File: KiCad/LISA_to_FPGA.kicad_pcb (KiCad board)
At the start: 2 copper layers, 77.7 x 29.5 mm, 16 parts, among them J1 Conn_01x02, J2 Conn_01x02, J3 Conn_01x40, U1 LM1117-3.3, U2 74LVC245A, U3 74LVC245A, U5 LISA

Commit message: more place and route
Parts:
- removed J3: Conn_01x40, Connector_FFC-FPC:Hirose_FH12-40S-0.5SH_1x40-1MP_P0.50mm_Horizontal
- removed the REF** at (133.3, 95.8)
- added U4: 74LVC245A, Package_SO:TSSOP-20_4.4x6.5mm_P0.65mm, F.Cu at (187.6, 85.9)
- added U6: LISA, LISA_to_FPGA:PLCC-84_THT-Socket-HAT, B.Cu at (166.8, 90.4)
- C3: footprint Capacitor_SMD:C_0805_2012Metric_Pad1.15x1.40mm_HandSolder -> Capacitor_SMD:C_0603_1608Metric_Pad1.08x0.95mm_HandSolder; moved to F.Cu
- C4, C5: footprint Capacitor_SMD:C_0805_2012Metric_Pad1.15x1.40mm_HandSolder -> Capacitor_SMD:C_0603_1608Metric_Pad1.08x0.95mm_HandSolder
- C6: footprint Capacitor_SMD:C_0805_2012Metric_Pad1.18x1.45mm_HandSolder -> Capacitor_SMD:C_0603_1608Metric_Pad1.08x0.95mm_HandSolder
- J1: value Conn_01x02 -> Conn_01x03; footprint Connector_PinHeader_2.54mm:PinHeader_1x02_P2.54mm_Horizontal -> Connector_PinHeader_2.54mm:PinHeader_1x03_P2.54mm_Horizontal
- J2: value Conn_01x02 -> Conn_01x40; footprint Connector_PinHeader_2.54mm:PinHeader_1x02_P2.54mm_Horizontal -> Connector_FFC-FPC:Hirose_FH12-40S-0.5SH_1x40-1MP_P0.50mm_Horizontal
- U5: value LISA -> 74LVC245A; footprint Package_LCC:PLCC-84_THT-Socket -> Package_SO:TSSOP-20_4.4x6.5mm_P0.65mm; moved to F.Cu
- moved C3 51.1 mm to (193.0, 99.0)
- moved C6 45.0 mm to (189.6, 73.5)
- moved C4 39.3 mm to (193.0, 92.3), turned to 90 degrees
- moved U2 39.1 mm to (187.6, 100.9)
- moved U1 38.6 mm to (191.8, 89.7)
- moved U3 36.5 mm to (187.6, 93.4)
- moved REF** 36.0 mm to (234.3, 93.4)
- moved C5 29.9 mm to (193.0, 84.0), turned to 90 degrees
- moved R1 23.2 mm to (193.9, 104.3)
- moved U5 13.4 mm to (187.6, 78.4), turned to 0 degrees
- moved J2 12.5 mm to (199.3, 94.4), turned to 90 degrees
- moved J1 5.59 mm to (191.3, 106.9)
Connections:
- J1 pad 2: Net-(J1-Pad2) -> HSYNC
- J2 pad 1: VSYNC -> /C14M_3V3
- J2 pad 2: HSYNC -> GND
- R1 pad 2: C14OUT -> C14OUT_3V3
- U2 pad 11: G7_3V3 -> C14OUT_3V3
- U2 pad 12: G6_3V3 -> VSYNC_3V3
- U2 pad 13: G5_3V3 -> HSYNC_3V3
- U2 pad 14: G4_3V3 -> PIXELSW_3V3
- U2 pad 15: R7_3V3 -> CSYNC_3V3
- U2 pad 16: R6_3V3 -> B7_3V3
- U2 pad 17: R5_3V3 -> B6_3V3
- U2 pad 18: R4_3V3 -> B5_3V3
- U2 pad 2: R4 -> B5
- U2 pad 3: R5 -> B6
- U2 pad 4: R6 -> B7
- U2 pad 5: R7 -> CSYNC
- U2 pad 6: G4 -> PIXELSW
- U2 pad 7: G5 -> HSYNC
- U2 pad 8: G6 -> VSYNC
- U2 pad 9: G7 -> C14OUT
- U3 pad 11: VSYNC_3V3 -> B4_3V3
- U3 pad 12: HSYNC_3V3 -> B3_3V3
- U3 pad 13: PIXELSW_3V3 -> B2_3V3
- U3 pad 14: CSYNC_3V3 -> B1_3V3
- U3 pad 15: B7_3V3 -> B0_3V3
- U3 pad 16: B6_3V3 -> G7_3V3
- U3 pad 17: B5_3V3 -> G6_3V3
- U3 pad 18: B4_3V3 -> G5_3V3
- U3 pad 2: B4 -> G5
- U3 pad 3: B5 -> G6
- U3 pad 4: B6 -> G7
- U3 pad 5: B7 -> B0
- U3 pad 6: CSYNC -> B1
- U3 pad 7: PIXELSW -> B2
- U3 pad 8: HSYNC -> B3
- U3 pad 9: VSYNC -> B4
- U5 pad 1: GND -> 3V3
- U5 pad 10: Net-(U5-Pad10) -> GND
- U5 pad 11: Net-(U5-Pad11) -> R4_3V3
- U5 pad 12: Net-(U5-Pad12) -> R3_3V3
- U5 pad 13: Net-(U5-Pad13) -> R2_3V3
- U5 pad 14: Net-(U5-Pad14) -> R1_3V3
- U5 pad 15: Net-(U5-Pad15) -> R0_3V3
- U5 pad 19: Net-(U5-Pad19) -> GND
- U5 pad 2: Net-(U5-Pad2) -> GND
- U5 pad 20: Net-(U5-Pad20) -> 3V3
- U5 pad 3: Net-(U5-Pad3) -> GND
- U5 pad 4: Net-(U5-Pad4) -> GND
- U5 pad 5: Net-(U5-Pad5) -> R0
- U5 pad 6: Net-(U5-Pad6) -> R1
- U5 pad 7: Net-(U5-Pad7) -> R2
- U5 pad 8: Net-(U5-Pad8) -> R3
- U5 pad 9: Net-(U5-Pad9) -> R4
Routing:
- net VCC: track 0.00 -> 69.7 mm
- net G4: track 0.00 -> 43.9 mm, vias 0 -> 1
- net G7: track 0.00 -> 40.5 mm, vias 0 -> 1
- net G3: track 0.00 -> 39.6 mm, vias 0 -> 1
- net R5: track 0.00 -> 36.3 mm
- net G5: track 0.00 -> 34.5 mm, vias 0 -> 1
- net R0: track 0.00 -> 33.8 mm
- net R3: track 0.00 -> 33.7 mm
- net G1: track 0.00 -> 33.7 mm, vias 0 -> 1
- net R7: track 0.00 -> 33.2 mm
- net G6: track 0.00 -> 33.2 mm, vias 0 -> 1
- net G2: track 0.00 -> 33.2 mm, vias 0 -> 1
- net B6: track 0.00 -> 33.0 mm, vias 0 -> 1
- net R4: track 0.00 -> 32.4 mm
- net R6: track 0.00 -> 32.4 mm
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- added copper zone on 3V3.Cu, net 3V3
- added copper zone on GND.Cu, net GND
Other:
- board size 77.7 x 29.5 mm -> 54.9 x 37 mm
- copper layers 2 -> 4
- board text added: "LISA to FPGA"
- board text removed: "CDAC"
- board text removed: "DENISE to FPGA"

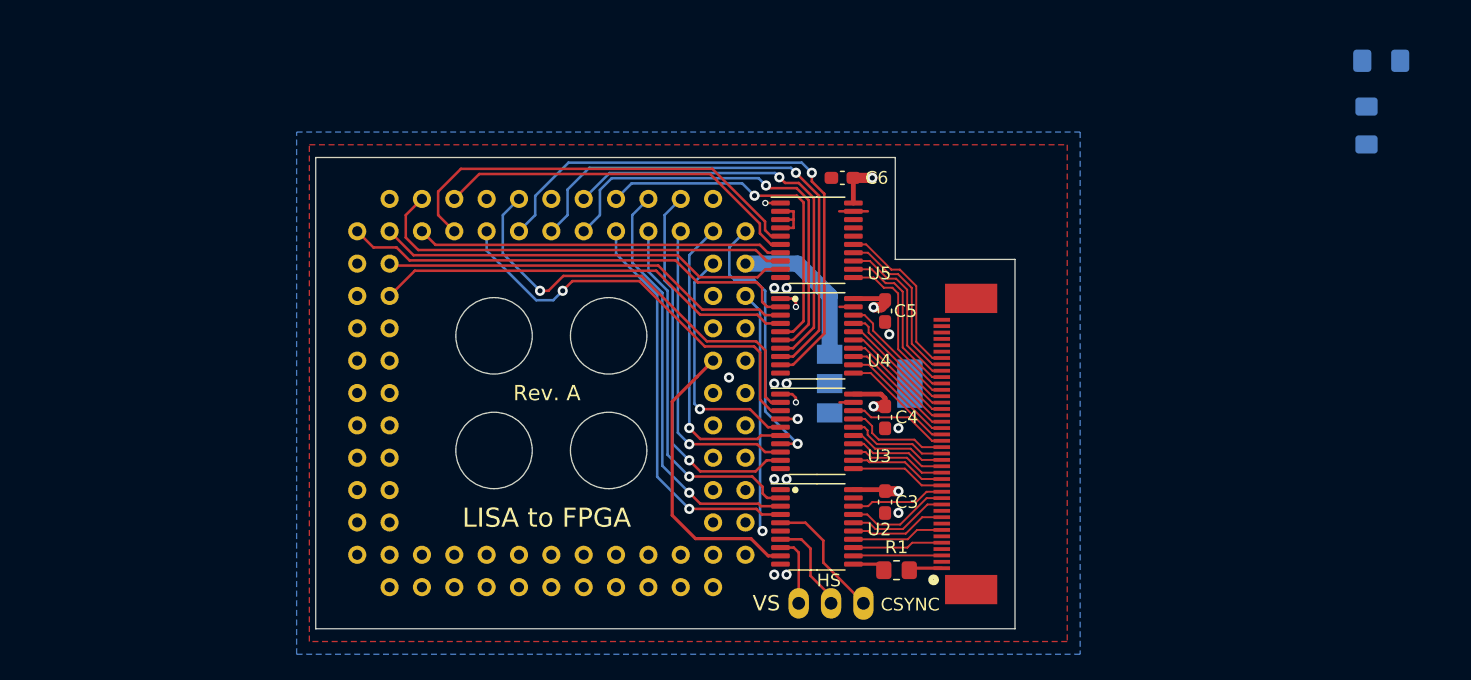
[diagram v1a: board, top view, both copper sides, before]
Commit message: routing and silkscreen fixes
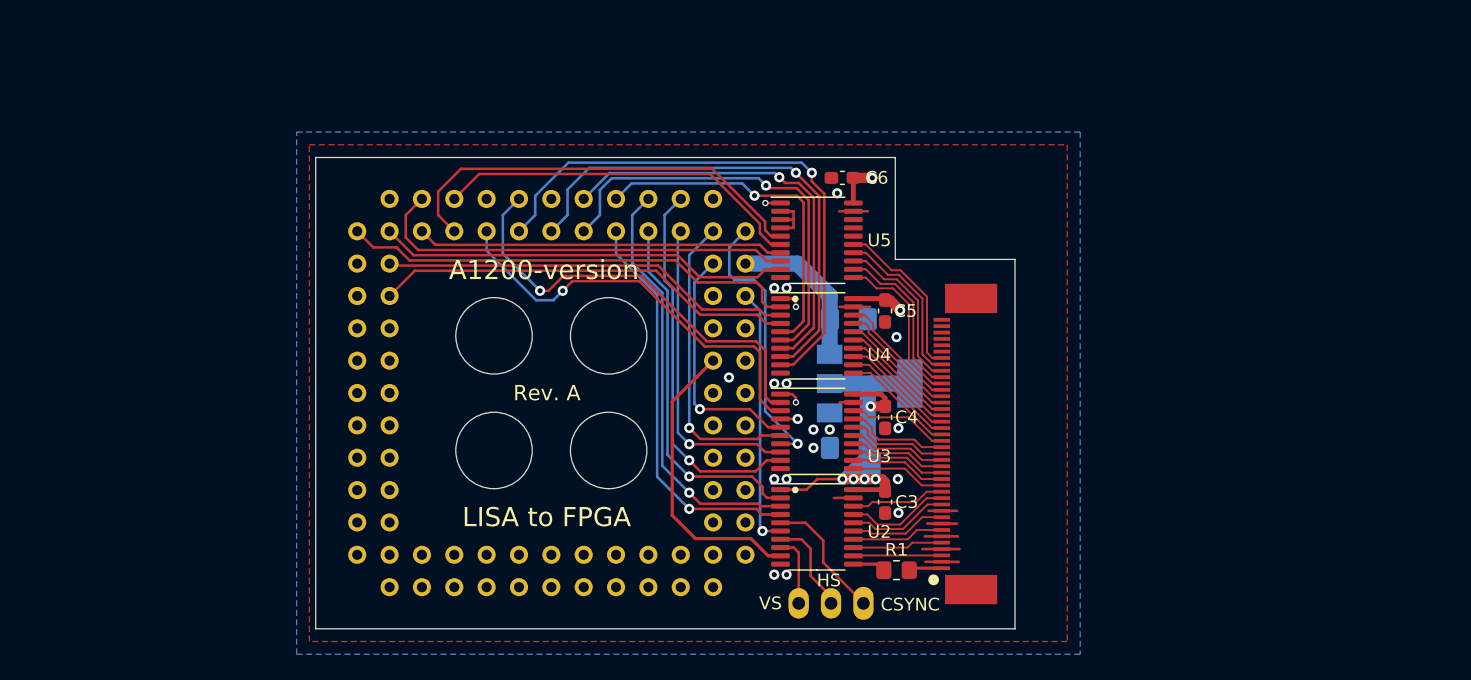
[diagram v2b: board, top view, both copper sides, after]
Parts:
- removed the REF** at (234.3, 93.4)
- added REF**: OSHW-Symbol_8.9x8mm_SilkScreen, Symbol:OSHW-Symbol_8.9x8mm_SilkScreen, B.Cu at (198.0, 98.0)
- moved C2 47.9 mm to (190.1, 94.7), turned to 0 degrees
- moved C1 46.5 mm to (190.1, 84.6), turned to 180 degrees
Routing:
- net 3V3: track 19.6 -> 54.0 mm, vias 7 -> 10
- net GND: track 8.82 -> 24.4 mm, vias 12 -> 17
- net PIXELSW: track 19.0 -> 20.4 mm
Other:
- board text added: "A1200-version"
- board text added: "HSYNC"
- board text added: "VSYNC"
